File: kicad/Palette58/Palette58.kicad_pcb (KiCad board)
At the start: 2 copper layers, 143.9 x 127.8 mm, 124 parts, among them SW1 MSK12C02-HB, SW2 TS-1187A-B-A-B

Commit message: change smd diode footprint to 323
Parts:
- D30: value (none) -> 1N5819
- LED1, LED10, LED11, LED12, LED13, LED14, LED15, LED16, LED17, LED18, LED19, LED2, LED20, LED21, LED22, LED23, LED24, LED25, LED26, LED27, LED28, LED29, LED3, LED4, LED5, LED6, LED7, LED8, LED9: value XINGLIGHTXL-1615RGBC-WS2812B -> (none); footprint LED_SMD:XINGLIGHT XL-1615RGBC-WS2812B -> WS2812B
- R1: footprint Resistor_SMD:R_0402_1005Metric -> Resistor
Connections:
- LED1 pad 1: VCC -> (no net)
- LED1 pad 2: Net-(LED1-DOUT) -> GND
- LED1 pad 3: B- -> (no net)
- LED1 pad 4: Net-(LED1-DIN) -> VCC
- LED10 pad 1: VCC -> (no net)
- LED10 pad 2: Net-(LED10-DOUT) -> GND
- LED10 pad 3: B- -> (no net)
- LED10 pad 4: Net-(LED10-DIN) -> VCC
- LED11 pad 1: VCC -> (no net)
- LED11 pad 2: Net-(LED11-DOUT) -> GND
- LED11 pad 3: B- -> (no net)
- LED11 pad 4: Net-(LED11-DIN) -> VCC
- LED12 pad 1: VCC -> (no net)
- LED12 pad 2: Net-(LED12-DOUT) -> GND
- LED12 pad 3: B- -> (no net)
- LED12 pad 4: Net-(LED12-DIN) -> VCC
- LED13 pad 1: VCC -> (no net)
- LED13 pad 2: Net-(LED13-DOUT) -> GND
- LED13 pad 3: B- -> (no net)
- LED13 pad 4: Net-(LED13-DIN) -> VCC
- LED14 pad 1: VCC -> (no net)
- LED14 pad 2: Net-(LED10-DIN) -> GND
- LED14 pad 3: B- -> (no net)
- LED14 pad 4: Net-(LED14-DIN) -> VCC
- LED15 pad 1: VCC -> (no net)
- LED15 pad 2: Net-(LED15-DOUT) -> GND
- LED15 pad 3: B- -> (no net)
- LED15 pad 4: Net-(LED11-DOUT) -> VCC
- LED16 pad 1: VCC -> (no net)
- LED16 pad 2: Net-(LED12-DIN) -> GND
- LED16 pad 3: B- -> (no net)
- LED16 pad 4: unconnected-(LED16-DIN-Pad4) -> VCC
- LED17 pad 1: VCC -> (no net)
- LED17 pad 2: Net-(LED17-DOUT) -> GND
- LED17 pad 3: B- -> (no net)
- LED17 pad 4: Net-(LED13-DOUT) -> VCC
- LED18 pad 1: VCC -> (no net)
- LED18 pad 2: Net-(LED14-DIN) -> GND
- LED18 pad 3: B- -> (no net)
- LED18 pad 4: Net-(LED18-DIN) -> VCC
- LED19 pad 1: VCC -> (no net)
- LED19 pad 2: Net-(LED19-DOUT) -> GND
- LED19 pad 3: B- -> (no net)
- LED19 pad 4: Net-(LED15-DOUT) -> VCC
- LED2 pad 1: VCC -> (no net)
- LED2 pad 2: Net-(LED1-DIN) -> GND
- LED2 pad 3: B- -> (no net)
- LED2 pad 4: Net-(LED2-DIN) -> VCC
- LED20 pad 1: VCC -> (no net)
- LED20 pad 2: unconnected-(LED20-DOUT-Pad2) -> GND
- LED20 pad 3: B- -> (no net)
- LED20 pad 4: Net-(LED20-DIN) -> VCC
- LED21 pad 1: VCC -> (no net)
- LED21 pad 2: Net-(LED21-DOUT) -> GND
- LED21 pad 3: B- -> (no net)
- LED21 pad 4: Net-(LED17-DOUT) -> VCC
- LED22 pad 1: VCC -> (no net)
- LED22 pad 2: Net-(LED18-DIN) -> GND
- LED22 pad 3: B- -> (no net)
- LED22 pad 4: Net-(LED22-DIN) -> VCC
- LED23 pad 1: VCC -> (no net)
- LED23 pad 2: Net-(LED22-DIN) -> GND
- LED23 pad 3: B- -> (no net)
- LED23 pad 4: Net-(LED19-DOUT) -> VCC
- LED24 pad 1: VCC -> (no net)
- LED24 pad 2: Net-(LED20-DIN) -> GND
- LED24 pad 3: B- -> (no net)
- LED24 pad 4: Net-(LED24-DIN) -> VCC
- LED25 pad 1: VCC -> (no net)
- LED25 pad 2: Net-(LED25-DOUT) -> GND
- LED25 pad 3: B- -> (no net)
- LED25 pad 4: Net-(LED21-DOUT) -> VCC
- LED26 pad 1: VCC -> (no net)
- LED26 pad 2: Net-(LED26-DOUT) -> GND
- LED26 pad 3: B- -> (no net)
- LED26 pad 4: Net-(LED25-DOUT) -> VCC
- LED27 pad 1: VCC -> (no net)
- LED27 pad 2: Net-(LED27-DOUT) -> GND
- LED27 pad 3: B- -> (no net)
- LED27 pad 4: Net-(LED26-DOUT) -> VCC
- LED28 pad 1: VCC -> (no net)
- LED28 pad 2: Net-(LED28-DOUT) -> GND
- LED28 pad 3: B- -> (no net)
- LED28 pad 4: Net-(LED27-DOUT) -> VCC
- LED29 pad 1: VCC -> (no net)
- LED29 pad 2: unconnected-(LED29-DOUT-Pad2) -> GND
- LED29 pad 3: B- -> (no net)
- LED29 pad 4: Net-(LED28-DOUT) -> VCC
- LED3 pad 1: VCC -> (no net)
- LED3 pad 2: Net-(LED3-DOUT) -> GND
- LED3 pad 3: B- -> (no net)
- LED3 pad 4: Net-(LED3-DIN) -> VCC
- LED4 pad 1: VCC -> (no net)
- LED4 pad 2: Net-(LED3-DIN) -> GND
- LED4 pad 3: B- -> (no net)
- LED4 pad 4: Net-(LED4-DIN) -> VCC
- LED5 pad 1: VCC -> (no net)
- LED5 pad 2: Net-(LED5-DOUT) -> GND
- LED5 pad 3: B- -> (no net)
- LED5 pad 4: Net-(LED1-DOUT) -> VCC
- LED6 pad 1: VCC -> (no net)
- LED6 pad 2: Net-(LED2-DIN) -> GND
- LED6 pad 3: B- -> (no net)
- LED6 pad 4: Net-(LED10-DOUT) -> VCC
- LED7 pad 1: VCC -> (no net)
- LED7 pad 2: Net-(LED11-DIN) -> GND
- LED7 pad 3: B- -> (no net)
- LED7 pad 4: Net-(LED3-DOUT) -> VCC
- LED8 pad 1: VCC -> (no net)
- LED8 pad 2: Net-(LED4-DIN) -> GND
- LED8 pad 3: B- -> (no net)
- LED8 pad 4: Net-(LED12-DOUT) -> VCC
- LED9 pad 1: VCC -> (no net)
- LED9 pad 2: Net-(LED13-DIN) -> GND
- LED9 pad 3: B- -> (no net)
- LED9 pad 4: Net-(LED5-DOUT) -> VCC
- R1 pad 1: Net-(LED24-DIN) -> (no net)
- R1 pad 2: P0.06 -> (no net)
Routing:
- net GND: vias 29 -> 58
- net B-: vias 29 -> 0
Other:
- net class Default added: clearance 0.2, trace_width 0.25, via_dia 0.8, via_drill 0.4

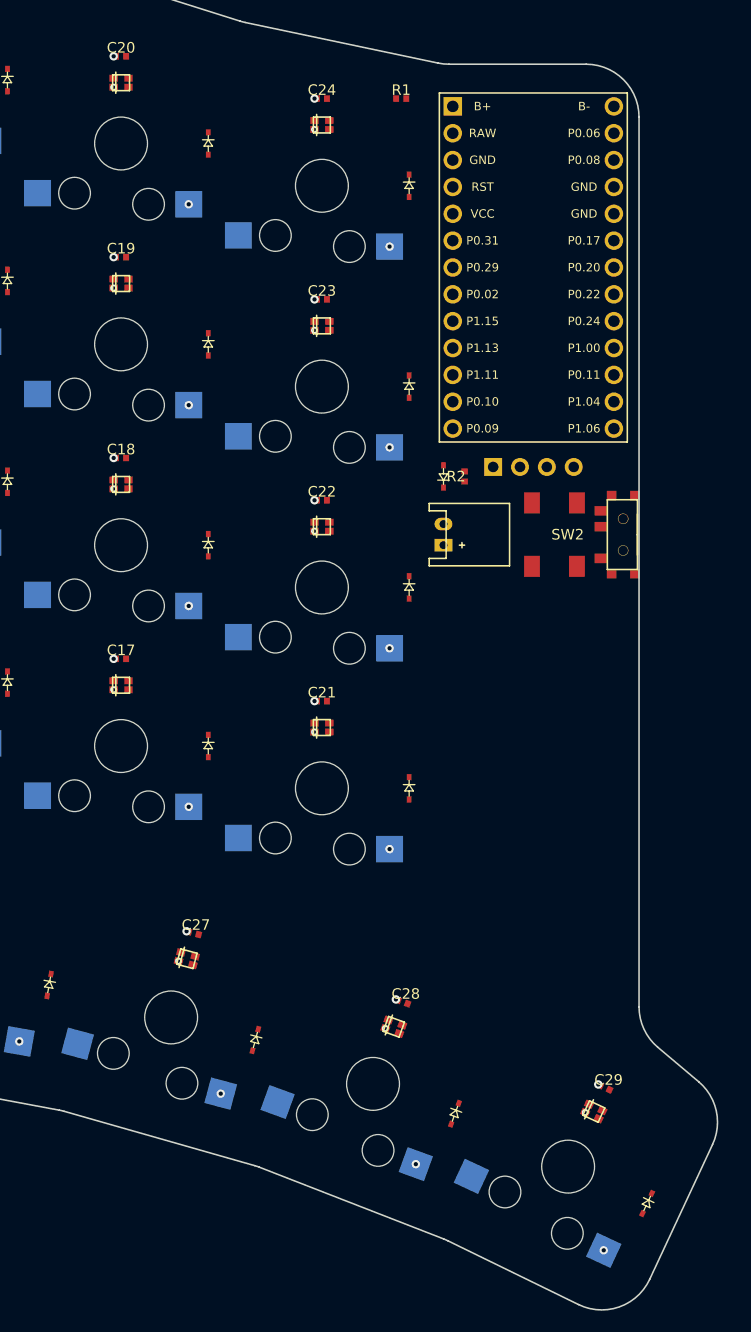
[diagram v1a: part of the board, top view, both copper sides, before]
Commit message: straighten mirrored edge
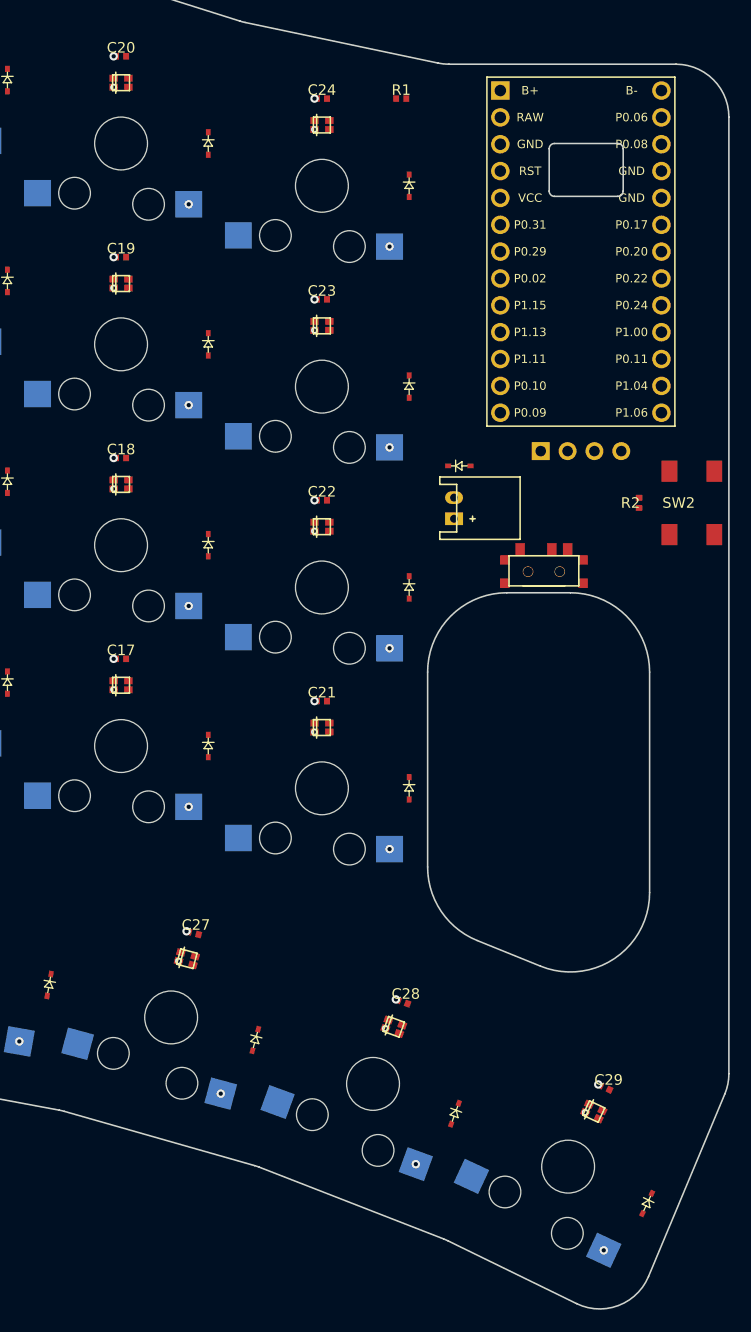
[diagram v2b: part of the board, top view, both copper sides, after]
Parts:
- moved R2 16.7 mm to (125.0, -40.5)
- moved SW2 13.3 mm to (130.0, -40.5), turned to 90 degrees
- moved SW1 8.28 mm to (116.0, -34.0), turned to 180 degrees
- moved MCU1 4.74 mm to (119.5, -63.0)
- moved OLED1 4.74 mm to (125.5, -47.0)
- moved JST1 2.69 mm to (107.5, -40.0)
- moved D30 1.80 mm to (108.0, -44.0), turned to 0 degrees
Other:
- board size 143.9 x 127.8 mm -> 145 x 127.8 mm

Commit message: Reflect board
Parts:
- added C30: 100nF, Capacitor, F.Cu at (267.0, -8.25)
- added C31: 100nF, Capacitor, F.Cu at (267.0, -27.2)
- added C32: 100nF, Capacitor, F.Cu at (267.0, -46.2)
- added C33: 100nF, Capacitor, F.Cu at (267.0, -65.2)
- added C34: 100nF, Capacitor, F.Cu at (248.0, -13.2)
- added C35: 100nF, Capacitor, F.Cu at (248.0, -32.2)
- added C36: 100nF, Capacitor, F.Cu at (248.0, -51.2)
- added C37: 100nF, Capacitor, F.Cu at (248.0, -70.2)
- added C38: 100nF, Capacitor, F.Cu at (229.0, -28.2)
- added C39: 100nF, Capacitor, F.Cu at (229.0, -47.2)
- added C40: 100nF, Capacitor, F.Cu at (229.0, -66.2)
- added C41: 100nF, Capacitor, F.Cu at (229.0, -85.2)
- added C42: 100nF, Capacitor, F.Cu at (210.0, -31.8)
- added C43: 100nF, Capacitor, F.Cu at (210.0, -50.8)
- added C44: 100nF, Capacitor, F.Cu at (210.0, -69.8)
- added C45: 100nF, Capacitor, F.Cu at (210.0, -88.8)
- added C46: 100nF, Capacitor, F.Cu at (191.0, -25.8)
- added C47: 100nF, Capacitor, F.Cu at (191.0, -44.8)
- added C48: 100nF, Capacitor, F.Cu at (191.0, -63.8)
- added C49: 100nF, Capacitor, F.Cu at (191.0, -82.8)
- added C50: 100nF, Capacitor, F.Cu at (172.0, -21.8)
- added C51: 100nF, Capacitor, F.Cu at (172.0, -40.8)
- added C52: 100nF, Capacitor, F.Cu at (172.0, -59.8)
- added C53: 100nF, Capacitor, F.Cu at (172.0, -78.8)
- added C54: 100nF, Capacitor, F.Cu at (225.3, -7.22)
- added C55: 100nF, Capacitor, F.Cu at (204.5, -4.46)
- added C56: 100nF, Capacitor, F.Cu at (184.1, 0.20)
- added C57: 100nF, Capacitor, F.Cu at (164.3, 6.71)
- added C58: 100nF, Capacitor, F.Cu at (145.2, 14.8)
- added D31: 1N4148, ComboDiode, F.Cu at (275.2, -19.0)
- added D32: 1N4148, ComboDiode, F.Cu at (275.2, -38.0)
- added D33: 1N4148, ComboDiode, F.Cu at (275.2, -57.0)
- added D34: 1N4148, ComboDiode, F.Cu at (256.2, -5.00)
- added D35: 1N4148, ComboDiode, F.Cu at (256.2, -24.0)
- added D36: 1N4148, ComboDiode, F.Cu at (256.2, -43.0)
- added D37: 1N4148, ComboDiode, F.Cu at (256.2, -62.0)
- added D38: 1N4148, ComboDiode, F.Cu at (237.2, -20.0)
- added D39: 1N4148, ComboDiode, F.Cu at (237.2, -39.0)
- added D40: 1N4148, ComboDiode, F.Cu at (237.2, -58.0)
- added D41: 1N4148, ComboDiode, F.Cu at (237.2, -77.0)
- added D42: 1N4148, ComboDiode, F.Cu at (218.2, -23.5)
- added D43: 1N4148, ComboDiode, F.Cu at (218.2, -42.5)
- added D44: 1N4148, ComboDiode, F.Cu at (218.2, -61.5)
- added D45: 1N4148, ComboDiode, F.Cu at (218.2, -80.5)
- added D46: 1N4148, ComboDiode, F.Cu at (199.2, -17.5)
- added D47: 1N4148, ComboDiode, F.Cu at (199.2, -36.5)
- added D48: 1N4148, ComboDiode, F.Cu at (199.2, -55.5)
- added D49: 1N4148, ComboDiode, F.Cu at (199.2, -74.5)
- added D50: 1N4148, ComboDiode, F.Cu at (180.2, -13.5)
- added D51: 1N4148, ComboDiode, F.Cu at (180.2, -32.5)
- added D52: 1N4148, ComboDiode, F.Cu at (180.2, -51.5)
- added D53: 1N4148, ComboDiode, F.Cu at (180.2, -70.5)
- added D54: 1N4148, ComboDiode, F.Cu at (234.2, 0.28)
- added D55: 1N4148, ComboDiode, F.Cu at (214.1, 2.24)
- added D56: 1N4148, ComboDiode, F.Cu at (194.2, 6.04)
- added D57: 1N4148, ComboDiode, F.Cu at (174.9, 11.6)
- added D58: 1N4148, ComboDiode, F.Cu at (156.2, 18.8)
- added D59: 1N5819, ComboDiode, F.Cu at (108.0, -44.0)
- added D60: 1N5819, ComboDiode, F.Cu at (159.0, -44.0)
- added JST2: , JST_PH_S2B-PH-K_02x2.00mm_Angled, F.Cu at (159.5, -40.0)
- added LED30: XINGLIGHTXL-1615RGBC-WS2812B, LED_SMD:XINGLIGHT XL-1615RGBC-WS2812B, F.Cu at (267.0, -5.75)
- added LED31: XINGLIGHTXL-1615RGBC-WS2812B, LED_SMD:XINGLIGHT XL-1615RGBC-WS2812B, F.Cu at (267.0, -24.8)
- added LED32: XINGLIGHTXL-1615RGBC-WS2812B, LED_SMD:XINGLIGHT XL-1615RGBC-WS2812B, F.Cu at (267.0, -43.8)
- added LED33: XINGLIGHTXL-1615RGBC-WS2812B, LED_SMD:XINGLIGHT XL-1615RGBC-WS2812B, F.Cu at (267.0, -62.8)
- added LED34: XINGLIGHTXL-1615RGBC-WS2812B, LED_SMD:XINGLIGHT XL-1615RGBC-WS2812B, F.Cu at (248.0, -10.8)
- added LED35: XINGLIGHTXL-1615RGBC-WS2812B, LED_SMD:XINGLIGHT XL-1615RGBC-WS2812B, F.Cu at (248.0, -29.8)
- added LED36: XINGLIGHTXL-1615RGBC-WS2812B, LED_SMD:XINGLIGHT XL-1615RGBC-WS2812B, F.Cu at (248.0, -48.8)
- added LED37: XINGLIGHTXL-1615RGBC-WS2812B, LED_SMD:XINGLIGHT XL-1615RGBC-WS2812B, F.Cu at (248.0, -67.8)
- added LED38: XINGLIGHTXL-1615RGBC-WS2812B, LED_SMD:XINGLIGHT XL-1615RGBC-WS2812B, F.Cu at (229.0, -25.8)
- added LED39: XINGLIGHTXL-1615RGBC-WS2812B, LED_SMD:XINGLIGHT XL-1615RGBC-WS2812B, F.Cu at (229.0, -44.8)
- added LED40: XINGLIGHTXL-1615RGBC-WS2812B, LED_SMD:XINGLIGHT XL-1615RGBC-WS2812B, F.Cu at (229.0, -63.8)
- added LED41: XINGLIGHTXL-1615RGBC-WS2812B, LED_SMD:XINGLIGHT XL-1615RGBC-WS2812B, F.Cu at (229.0, -82.8)
- added LED42: XINGLIGHTXL-1615RGBC-WS2812B, LED_SMD:XINGLIGHT XL-1615RGBC-WS2812B, F.Cu at (210.0, -29.2)
- added LED43: XINGLIGHTXL-1615RGBC-WS2812B, LED_SMD:XINGLIGHT XL-1615RGBC-WS2812B, F.Cu at (210.0, -48.2)
- added LED44: XINGLIGHTXL-1615RGBC-WS2812B, LED_SMD:XINGLIGHT XL-1615RGBC-WS2812B, F.Cu at (210.0, -67.2)
- added LED45: XINGLIGHTXL-1615RGBC-WS2812B, LED_SMD:XINGLIGHT XL-1615RGBC-WS2812B, F.Cu at (210.0, -86.2)
- added LED46: XINGLIGHTXL-1615RGBC-WS2812B, LED_SMD:XINGLIGHT XL-1615RGBC-WS2812B, F.Cu at (191.0, -23.2)
- added LED47: XINGLIGHTXL-1615RGBC-WS2812B, LED_SMD:XINGLIGHT XL-1615RGBC-WS2812B, F.Cu at (191.0, -42.2)
- added LED48: XINGLIGHTXL-1615RGBC-WS2812B, LED_SMD:XINGLIGHT XL-1615RGBC-WS2812B, F.Cu at (191.0, -61.2)
- added LED49: XINGLIGHTXL-1615RGBC-WS2812B, LED_SMD:XINGLIGHT XL-1615RGBC-WS2812B, F.Cu at (191.0, -80.2)
- added LED50: XINGLIGHTXL-1615RGBC-WS2812B, LED_SMD:XINGLIGHT XL-1615RGBC-WS2812B, F.Cu at (172.0, -19.2)
- added LED51: XINGLIGHTXL-1615RGBC-WS2812B, LED_SMD:XINGLIGHT XL-1615RGBC-WS2812B, F.Cu at (172.0, -38.2)
- added LED52: XINGLIGHTXL-1615RGBC-WS2812B, LED_SMD:XINGLIGHT XL-1615RGBC-WS2812B, F.Cu at (172.0, -57.2)
- added LED53: XINGLIGHTXL-1615RGBC-WS2812B, LED_SMD:XINGLIGHT XL-1615RGBC-WS2812B, F.Cu at (172.0, -76.2)
- added LED54: XINGLIGHTXL-1615RGBC-WS2812B, LED_SMD:XINGLIGHT XL-1615RGBC-WS2812B, F.Cu at (225.5, -4.73)
- added LED55: XINGLIGHTXL-1615RGBC-WS2812B, LED_SMD:XINGLIGHT XL-1615RGBC-WS2812B, F.Cu at (204.9, -1.99)
- added LED56: XINGLIGHTXL-1615RGBC-WS2812B, LED_SMD:XINGLIGHT XL-1615RGBC-WS2812B, F.Cu at (184.8, 2.62)
- added LED57: XINGLIGHTXL-1615RGBC-WS2812B, LED_SMD:XINGLIGHT XL-1615RGBC-WS2812B, F.Cu at (165.2, 9.06)
- added LED58: XINGLIGHTXL-1615RGBC-WS2812B, LED_SMD:XINGLIGHT XL-1615RGBC-WS2812B, F.Cu at (146.3, 17.1)
- added MCU2: , nice!nanov2, F.Cu at (147.5, -63.0)
- added OLED2: OLED, lib:OLED_headers, F.Cu at (153.5, -47.0)
- added R3: 10kΩ, Resistor, F.Cu at (125.0, -40.5)
- added R4: 10kΩ, Resistor, F.Cu at (142.0, -40.5)
- added S30: , Gaeteron_low_profile, F.Cu at (267.0, 0.00)
- added S31: , Gaeteron_low_profile, F.Cu at (267.0, -19.0)
- added S32: , Gaeteron_low_profile, F.Cu at (267.0, -38.0)
- added S33: , Gaeteron_low_profile, F.Cu at (267.0, -57.0)
- added S34: , Gaeteron_low_profile, F.Cu at (248.0, -5.00)
- added S35: , Gaeteron_low_profile, F.Cu at (248.0, -24.0)
- added S36: , Gaeteron_low_profile, F.Cu at (248.0, -43.0)
- added S37: , Gaeteron_low_profile, F.Cu at (248.0, -62.0)
- added S38: , Gaeteron_low_profile, F.Cu at (229.0, -20.0)
- added S39: , Gaeteron_low_profile, F.Cu at (229.0, -39.0)
- added S40: , Gaeteron_low_profile, F.Cu at (229.0, -58.0)
- added S41: , Gaeteron_low_profile, F.Cu at (229.0, -77.0)
- added S42: , Gaeteron_low_profile, F.Cu at (210.0, -23.5)
- added S43: , Gaeteron_low_profile, F.Cu at (210.0, -42.5)
- added S44: , Gaeteron_low_profile, F.Cu at (210.0, -61.5)
- added S45: , Gaeteron_low_profile, F.Cu at (210.0, -80.5)
- added S46: , Gaeteron_low_profile, F.Cu at (191.0, -17.5)
- added S47: , Gaeteron_low_profile, F.Cu at (191.0, -36.5)
- added S48: , Gaeteron_low_profile, F.Cu at (191.0, -55.5)
- added S49: , Gaeteron_low_profile, F.Cu at (191.0, -74.5)
- added S50: , Gaeteron_low_profile, F.Cu at (172.0, -13.5)
- added S51: , Gaeteron_low_profile, F.Cu at (172.0, -32.5)
- added S52: , Gaeteron_low_profile, F.Cu at (172.0, -51.5)
- added S53: , Gaeteron_low_profile, F.Cu at (172.0, -70.5)
- added S54: , Gaeteron_low_profile, F.Cu at (226.0, 1.00)
- added S55: , Gaeteron_low_profile, F.Cu at (205.9, 3.67)
- added S56: , Gaeteron_low_profile, F.Cu at (186.3, 8.17)
- added S57: , Gaeteron_low_profile, F.Cu at (167.2, 14.5)
- added S58: , Gaeteron_low_profile, F.Cu at (148.7, 22.3)
- added SW3: TS-1187A-B-A-B, PushSwitch, F.Cu at (130.0, -40.5)
- added SW4: TS-1187A-B-A-B, PushSwitch, F.Cu at (137.0, -40.5)
- D30: value 1N5819 -> 1N4148
- LED1, LED10, LED11, LED12, LED13, LED14, LED15, LED16, LED17, LED18, LED19, LED2, LED20, LED21, LED22, LED23, LED24, LED25, LED26, LED27, LED28, LED29, LED3, LED4, LED5, LED6, LED7, LED8, LED9: value (none) -> XINGLIGHTXL-1615RGBC-WS2812B; footprint WS2812B -> LED_SMD:XINGLIGHT XL-1615RGBC-WS2812B
- R1: footprint Resistor -> Resistor_SMD:R_0402_1005Metric
- R2: value 10kΩ -> 330Ω; footprint Resistor -> Resistor_SMD:R_0402_1005Metric
- SW2: value TS-1187A-B-A-B -> MSK12C02-HB; footprint PushSwitch -> E73:SPDT_C128955
- moved D30 172.9 mm to (275.2, 0.00), turned to -90 degrees
- moved R2 51.5 mm to (159.5, -78.8), turned to 180 degrees
- moved SW2 22.0 mm to (151.0, -34.0), turned to 180 degrees
- moved R1 5.00 mm to (107.5, -78.8)
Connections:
- D30 pad 1: JST+ -> row_4
- D30 pad 2: B+ -> mirror_outer_bottom
- LED1 pad 1: (no net) -> VCC
- LED1 pad 2: GND -> Net-(LED1-DOUT)
- LED1 pad 3: (no net) -> GND
- LED1 pad 4: VCC -> Net-(LED1-DIN)
- LED10 pad 1: (no net) -> VCC
- LED10 pad 2: GND -> Net-(LED10-DOUT)
- LED10 pad 3: (no net) -> GND
- LED10 pad 4: VCC -> Net-(LED10-DIN)
- LED11 pad 1: (no net) -> VCC
- LED11 pad 2: GND -> Net-(LED11-DOUT)
- LED11 pad 3: (no net) -> GND
- LED11 pad 4: VCC -> Net-(LED11-DIN)
- LED12 pad 1: (no net) -> VCC
- LED12 pad 2: GND -> Net-(LED12-DOUT)
- LED12 pad 3: (no net) -> GND
- LED12 pad 4: VCC -> Net-(LED12-DIN)
- LED13 pad 1: (no net) -> VCC
- LED13 pad 2: GND -> Net-(LED13-DOUT)
- LED13 pad 3: (no net) -> GND
- LED13 pad 4: VCC -> Net-(LED13-DIN)
- LED14 pad 1: (no net) -> VCC
- LED14 pad 2: GND -> Net-(LED10-DIN)
- LED14 pad 3: (no net) -> GND
- LED14 pad 4: VCC -> Net-(LED14-DIN)
- LED15 pad 1: (no net) -> VCC
- LED15 pad 2: GND -> Net-(LED15-DOUT)
- LED15 pad 3: (no net) -> GND
- LED15 pad 4: VCC -> Net-(LED11-DOUT)
- LED16 pad 1: (no net) -> VCC
- LED16 pad 2: GND -> Net-(LED12-DIN)
- LED16 pad 3: (no net) -> GND
- LED16 pad 4: VCC -> unconnected-(LED16-DIN-Pad4)
- LED17 pad 1: (no net) -> VCC
- LED17 pad 2: GND -> Net-(LED17-DOUT)
- LED17 pad 3: (no net) -> GND
- LED17 pad 4: VCC -> Net-(LED13-DOUT)
- LED18 pad 1: (no net) -> VCC
- LED18 pad 2: GND -> Net-(LED14-DIN)
- LED18 pad 3: (no net) -> GND
- LED18 pad 4: VCC -> Net-(LED18-DIN)
- LED19 pad 1: (no net) -> VCC
- LED19 pad 2: GND -> Net-(LED19-DOUT)
- LED19 pad 3: (no net) -> GND
- LED19 pad 4: VCC -> Net-(LED15-DOUT)
- LED2 pad 1: (no net) -> VCC
- LED2 pad 2: GND -> Net-(LED1-DIN)
- LED2 pad 3: (no net) -> GND
- LED2 pad 4: VCC -> Net-(LED2-DIN)
- LED20 pad 1: (no net) -> VCC
- LED20 pad 2: GND -> unconnected-(LED20-DOUT-Pad2)
- LED20 pad 3: (no net) -> GND
- LED20 pad 4: VCC -> Net-(LED20-DIN)
- LED21 pad 1: (no net) -> VCC
- LED21 pad 2: GND -> Net-(LED21-DOUT)
- LED21 pad 3: (no net) -> GND
- LED21 pad 4: VCC -> Net-(LED17-DOUT)
- LED22 pad 1: (no net) -> VCC
- LED22 pad 2: GND -> Net-(LED18-DIN)
- LED22 pad 3: (no net) -> GND
- LED22 pad 4: VCC -> Net-(LED22-DIN)
- LED23 pad 1: (no net) -> VCC
- LED23 pad 2: GND -> Net-(LED22-DIN)
- LED23 pad 3: (no net) -> GND
- LED23 pad 4: VCC -> Net-(LED19-DOUT)
- LED24 pad 1: (no net) -> VCC
- LED24 pad 2: GND -> Net-(LED20-DIN)
- LED24 pad 3: (no net) -> GND
- LED24 pad 4: VCC -> Net-(LED24-DIN)
- LED25 pad 1: (no net) -> VCC
- LED25 pad 2: GND -> Net-(LED25-DOUT)
- LED25 pad 3: (no net) -> GND
- LED25 pad 4: VCC -> Net-(LED21-DOUT)
- LED26 pad 1: (no net) -> VCC
- LED26 pad 2: GND -> Net-(LED26-DOUT)
- LED26 pad 3: (no net) -> GND
- LED26 pad 4: VCC -> Net-(LED25-DOUT)
- LED27 pad 1: (no net) -> VCC
- LED27 pad 2: GND -> Net-(LED27-DOUT)
- LED27 pad 3: (no net) -> GND
- LED27 pad 4: VCC -> Net-(LED26-DOUT)
- LED28 pad 1: (no net) -> VCC
- LED28 pad 2: GND -> Net-(LED28-DOUT)
- LED28 pad 3: (no net) -> GND
- LED28 pad 4: VCC -> Net-(LED27-DOUT)
- LED29 pad 1: (no net) -> VCC
- LED29 pad 2: GND -> unconnected-(LED29-DOUT-Pad2)
- LED29 pad 3: (no net) -> GND
- LED29 pad 4: VCC -> Net-(LED28-DOUT)
- LED3 pad 1: (no net) -> VCC
- LED3 pad 2: GND -> Net-(LED3-DOUT)
- LED3 pad 3: (no net) -> GND
- LED3 pad 4: VCC -> Net-(LED3-DIN)
- LED4 pad 1: (no net) -> VCC
- LED4 pad 2: GND -> Net-(LED3-DIN)
- LED4 pad 3: (no net) -> GND
- LED4 pad 4: VCC -> Net-(LED4-DIN)
- LED5 pad 1: (no net) -> VCC
- LED5 pad 2: GND -> Net-(LED5-DOUT)
- LED5 pad 3: (no net) -> GND
- LED5 pad 4: VCC -> Net-(LED1-DOUT)
- LED6 pad 1: (no net) -> VCC
- LED6 pad 2: GND -> Net-(LED2-DIN)
- LED6 pad 3: (no net) -> GND
- LED6 pad 4: VCC -> Net-(LED10-DOUT)
- LED7 pad 1: (no net) -> VCC
- LED7 pad 2: GND -> Net-(LED11-DIN)
- LED7 pad 3: (no net) -> GND
- LED7 pad 4: VCC -> Net-(LED3-DOUT)
- LED8 pad 1: (no net) -> VCC
- LED8 pad 2: GND -> Net-(LED4-DIN)
- LED8 pad 3: (no net) -> GND
- LED8 pad 4: VCC -> Net-(LED12-DOUT)
- LED9 pad 1: (no net) -> VCC
- LED9 pad 2: GND -> Net-(LED13-DIN)
- LED9 pad 3: (no net) -> GND
- LED9 pad 4: VCC -> Net-(LED5-DOUT)
- R1 pad 1: (no net) -> Net-(LED24-DIN)
- R1 pad 2: (no net) -> P0.06
- R2 pad 1: VCC -> P0.06
- R2 pad 2: RST -> Net-(LED53-DIN)
- SW2 pad 1: RST -> JST+
- SW2 pad 2: RST -> B+
- SW2 pad 3: GND -> (no net)
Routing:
- net mirror_ring_top: vias 0 -> 1
- net mirror_ring_num: vias 0 -> 1
- net mirror_ring_home: vias 0 -> 1
- net mirror_ring_bottom: vias 0 -> 1
- net mirror_pinky_top: vias 0 -> 1
- net mirror_pinky_num: vias 0 -> 1
- net mirror_pinky_home: vias 0 -> 1
- net mirror_pinky_bottom: vias 0 -> 1
- net mirror_outer_top: vias 0 -> 1
- net mirror_outer_num: vias 0 -> 1
- net mirror_outer_home: vias 0 -> 1
- net mirror_outer_cluster: vias 0 -> 1
- net mirror_outer_bottom: vias 0 -> 1
- net mirror_outer-3_cluster: vias 0 -> 1
- net mirror_outer-2_cluster: vias 0 -> 1
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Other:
- board size 145 x 127.8 mm -> 290 x 127.8 mm
- net class Default removed

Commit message: Route simple routes
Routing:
- net col_6: track 0.00 -> 114.0 mm
- net col_5: track 0.00 -> 114.0 mm
- net col_4: track 0.00 -> 114.0 mm
- net col_3: track 0.00 -> 114.0 mm
- net col_2: track 0.00 -> 114.0 mm
- net col_1: track 0.00 -> 114.0 mm
- net JST+: track 0.00 -> 32.2 mm
- net B+: track 0.00 -> 21.6 mm
- net RST: track 0.00 -> 19.8 mm
- net SCL: track 0.00 -> 17.8 mm
- net SDA: track 0.00 -> 10.6 mm
- net mirror_outer_home: track 0.00 -> 5.46 mm
- net mirror_outer_top: track 0.00 -> 5.46 mm
- net mirror_outer_num: track 0.00 -> 5.46 mm
- net mirror_outer_bottom: track 0.00 -> 5.46 mm
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
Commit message: Route left half
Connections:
- LED16 pad 4: unconnected-(LED16-DIN-Pad4) -> Net-(LED16-DIN)
- LED20 pad 2: unconnected-(LED20-DOUT-Pad2) -> Net-(LED16-DIN)
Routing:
- net row_4: track 0.00 -> 177.1 mm
- net row_5: track 0.00 -> 170.6 mm
- net row_3: track 0.00 -> 159.6 mm
- net row_2: track 0.00 -> 147.8 mm
- net col_2: track 114.0 -> 259.5 mm
- net row_1: track 0.00 -> 145.0 mm
- net col_1: track 114.0 -> 257.9 mm
- net col_3: track 114.0 -> 243.6 mm
- net col_4: track 114.0 -> 223.1 mm
- net col_5: track 114.0 -> 205.1 mm
- net col_6: track 114.0 -> 187.4 mm
- net Net-(LED21-DOUT): track 0.00 -> 58.5 mm, vias 0 -> 2
- net B+: track 21.6 -> 59.9 mm, vias 0 -> 1
- net Net-(LED5-DOUT): track 0.00 -> 34.2 mm, vias 0 -> 2
- net Net-(LED11-DIN): track 0.00 -> 29.8 mm, vias 0 -> 2
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- added copper zone on B.Cu, net GND
- added copper zone on F.Cu, net VCC

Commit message: Finish Routing
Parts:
- turned R2 to 0 degrees
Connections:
- LED30 pad 2: unconnected-(LED30-DOUT-Pad2) -> Net-(LED30-DOUT)
- LED31 pad 2: unconnected-(LED31-DOUT-Pad2) -> Net-(LED30-DIN)
- LED34 pad 2: unconnected-(LED34-DOUT-Pad2) -> Net-(LED34-DOUT)
- LED34 pad 4: unconnected-(LED34-DIN-Pad4) -> Net-(LED30-DOUT)
- LED38 pad 2: unconnected-(LED38-DOUT-Pad2) -> Net-(LED38-DOUT)
- LED38 pad 4: unconnected-(LED38-DIN-Pad4) -> Net-(LED34-DOUT)
- LED42 pad 2: unconnected-(LED42-DOUT-Pad2) -> Net-(LED42-DOUT)
- LED42 pad 4: unconnected-(LED42-DIN-Pad4) -> Net-(LED38-DOUT)
- LED46 pad 2: unconnected-(LED46-DOUT-Pad2) -> Net-(LED46-DOUT)
- LED46 pad 4: unconnected-(LED46-DIN-Pad4) -> Net-(LED42-DOUT)
- LED50 pad 2: unconnected-(LED50-DOUT-Pad2) -> Net-(LED50-DOUT)
- LED50 pad 4: unconnected-(LED50-DIN-Pad4) -> Net-(LED46-DOUT)
- LED54 pad 4: Net-(LED30-DIN) -> Net-(LED50-DOUT)
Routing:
- net row_5: track 170.6 -> 359.9 mm
- net row_4: track 177.1 -> 362.9 mm
- net row_3: track 159.6 -> 313.6 mm
- net col_2: track 259.5 -> 409.0 mm
- net col_1: track 257.9 -> 405.2 mm
- net row_1: track 145.0 -> 289.7 mm
- net row_2: track 147.8 -> 292.4 mm
- net col_3: track 243.6 -> 374.1 mm
- net col_4: track 223.1 -> 336.2 mm
- net col_5: track 205.1 -> 300.1 mm
- net Net-(LED50-DOUT): track 0.00 -> 80.4 mm, vias 0 -> 2
- net col_6: track 187.4 -> 265.5 mm
- net GND: track 4.46 -> 45.0 mm, vias 120 -> 126
- net Net-(LED35-DIN): track 0.00 -> 35.1 mm
- net Net-(LED37-DIN): track 0.00 -> 32.9 mm
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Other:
- board text added: "V-Cut"
